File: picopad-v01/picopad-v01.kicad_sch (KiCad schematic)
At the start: 19 parts

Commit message: Complete the schematic
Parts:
- added D? (x17): SOD123, symbol Device:D_Small
- added MX?: NUMPAD_5, symbol MX-switches:MX-NoLED
- added MX?: NUMPAD_6, symbol MX-switches:MX-NoLED
- added MX?: NUMPAD_DOT, symbol MX-switches:MX-NoLED
- added MX?: NUMPAD_ASTERISK, symbol MX-switches:MX-NoLED
- added MX?: NUMPAD_PLUS, symbol MX-switches:MX-NoLED
- added MX?: NUMLOCK, symbol MX-switches:MX-NoLED
- added MX?: NUMPAD_1, symbol MX-switches:MX-NoLED
- added MX?: NUMPAD_7, symbol MX-switches:MX-NoLED
- added MX?: NUMPAD_MINUS, symbol MX-switches:MX-NoLED
- added MX?: NUMPAD_3, symbol MX-switches:MX-NoLED
- added MX?: NUMPAD_SLASH, symbol MX-switches:MX-NoLED
- added MX?: NUMPAD_4, symbol MX-switches:MX-NoLED
- added MX?: NUMPAD_ENTER, symbol MX-switches:MX-NoLED
- added MX?: NUMPAD_0, symbol MX-switches:MX-NoLED
- added MX?: NUMPAD_2, symbol MX-switches:MX-NoLED
- added MX?: NUMPAD_8, symbol MX-switches:MX-NoLED
- added MX?: NUMPAD_9, symbol MX-switches:MX-NoLED
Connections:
- net RGBLED: now reaches U?.11 (PB3)
- new net: D?.2 (A), MX?.2 (ROW) (x17)
- new net COL0: MX?.1 (COL), MX?.1 (COL), MX?.1 (COL), MX?.1 (COL), MX?.1 (COL), MX?.1 (COL), MX?.1 (COL), MX?.1 (COL), MX?.1 (COL), MX?.1 (COL), MX?.1 (COL), MX?.1 (COL), MX?.1 (COL), MX?.1 (COL), MX?.1 (COL), MX?.1 (COL), MX?.1 (COL)
- new net ROW0: D?.1 (K), D?.1 (K), D?.1 (K), D?.1 (K)
- new net ROW1: D?.1 (K), D?.1 (K), D?.1 (K)
- new net ROW2: D?.1 (K), D?.1 (K), D?.1 (K), D?.1 (K)
- new net ROW3: D?.1 (K), D?.1 (K), D?.1 (K)
- new net ROW4: D?.1 (K), D?.1 (K), D?.1 (K)

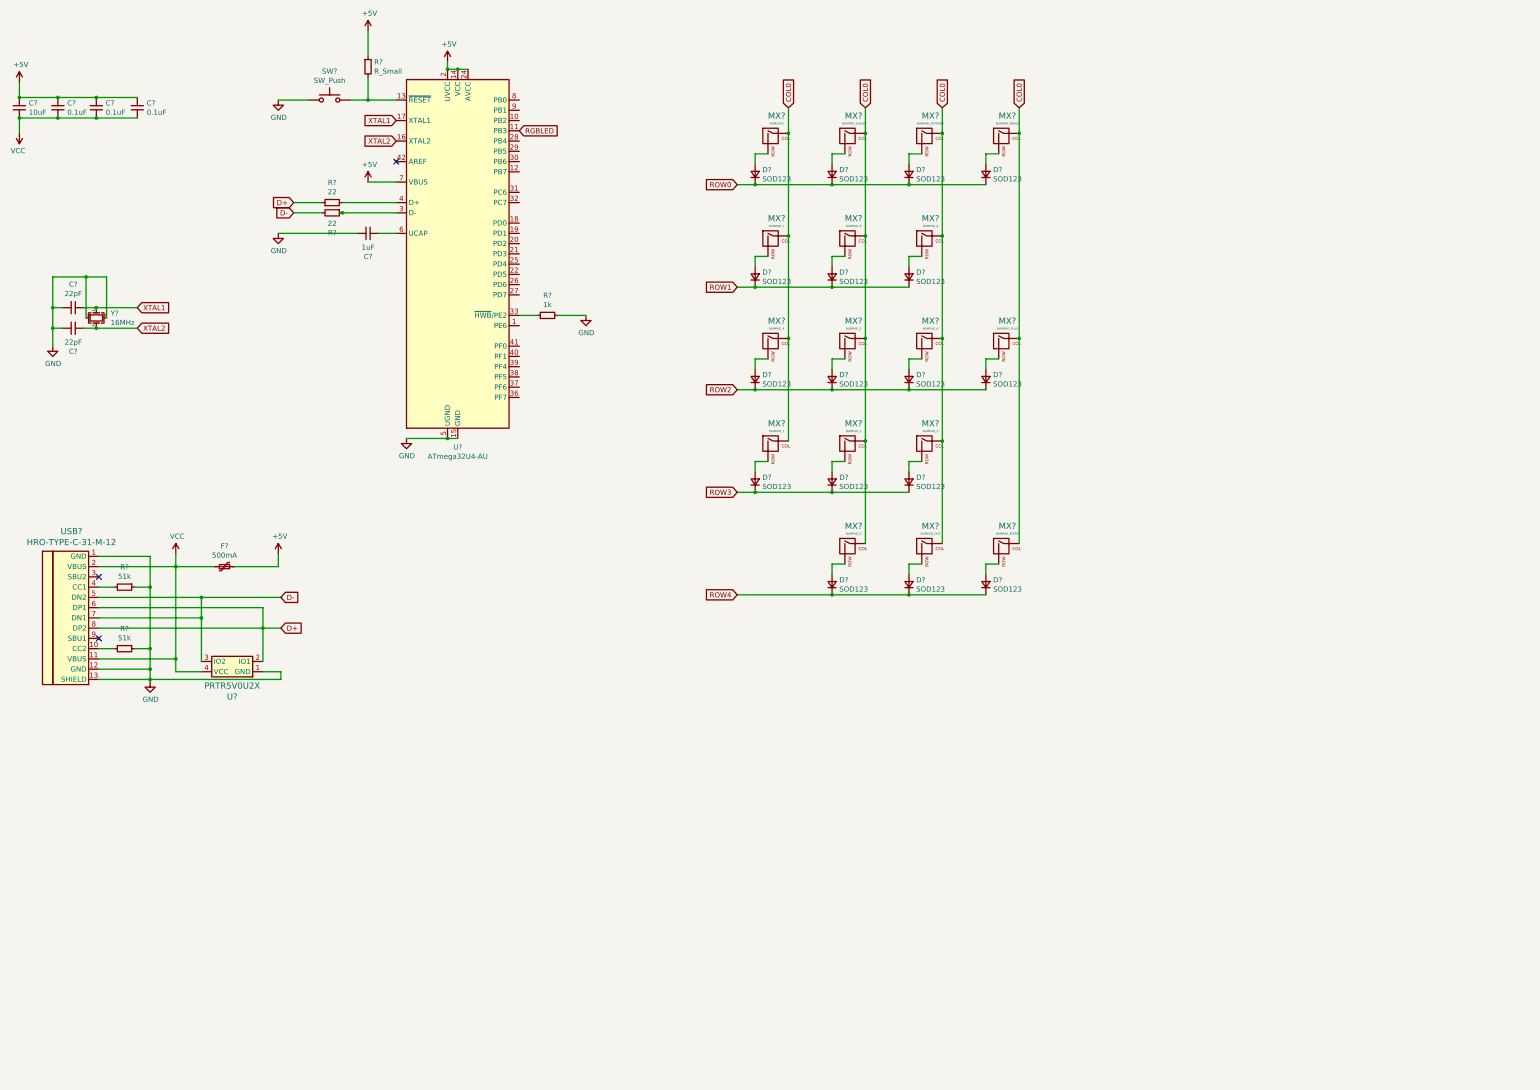
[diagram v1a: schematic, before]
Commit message: Add RGB backlight support
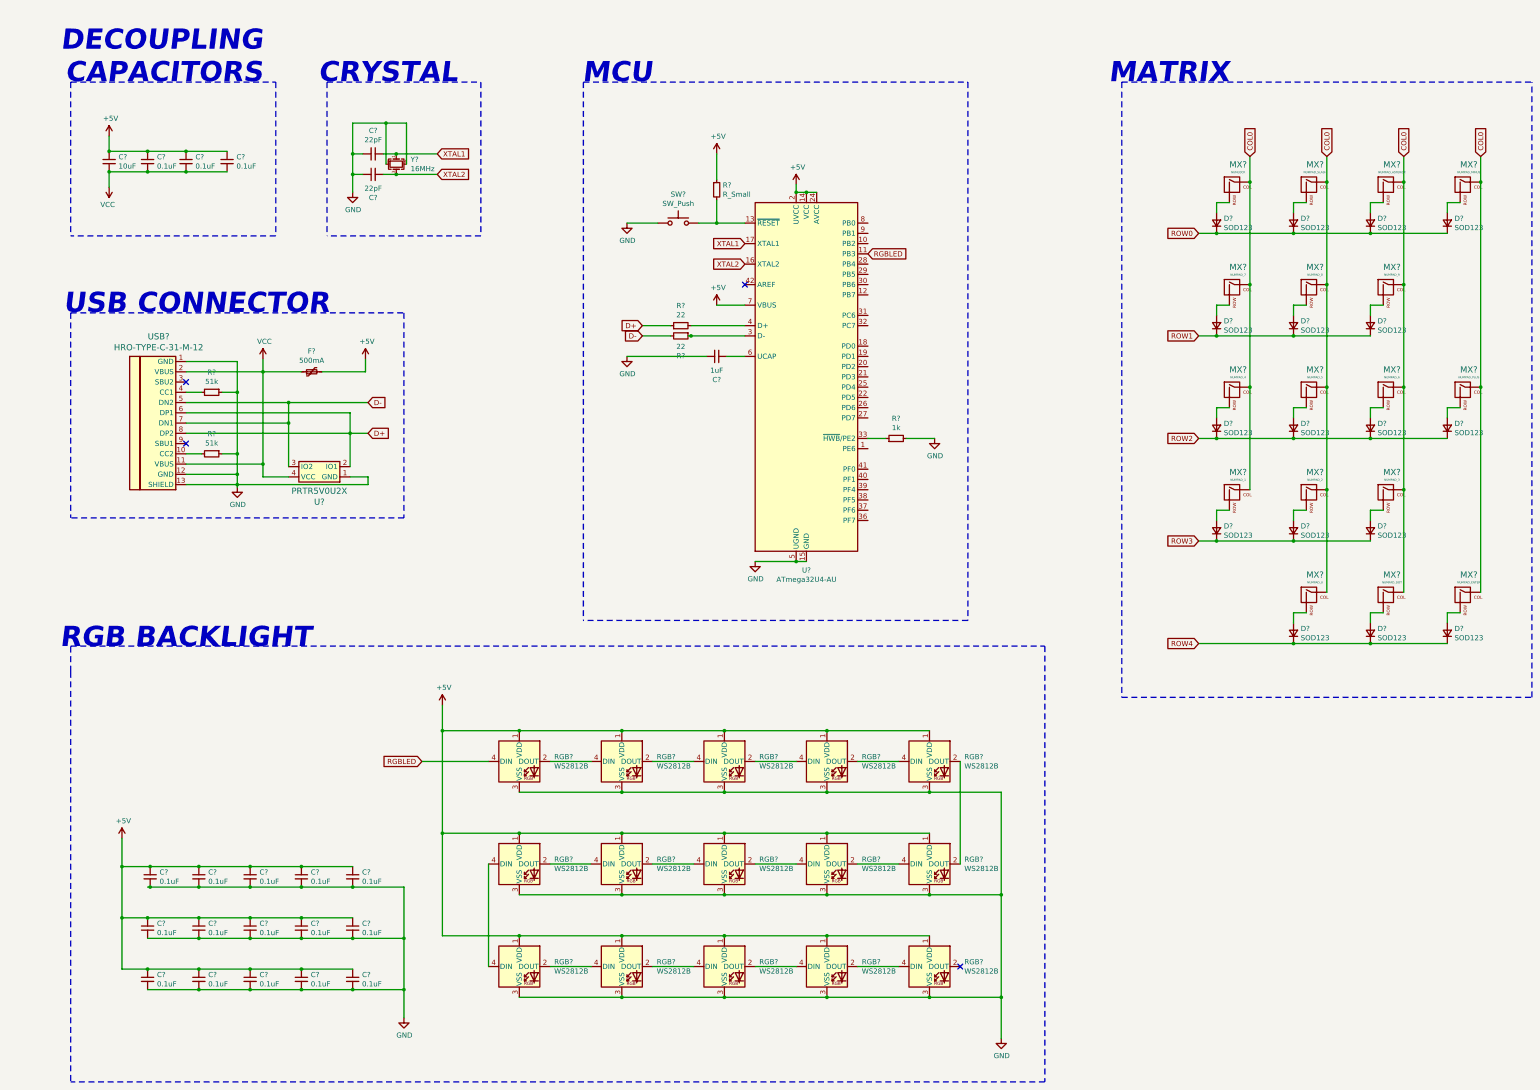
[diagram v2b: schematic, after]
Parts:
- added C? (x15): 0.1uF, symbol Device:C_Small
- added RGB? (x15): WS2812B, LED_SMD:LED_WS2812B_PLCC4_5.0x5.0mm_P3.2mm, symbol LED:WS2812B
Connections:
- net +5V: now also C?.1, C?.1, C?.1, C?.1, C?.1, C?.1, C?.1, C?.1, C?.1, C?.1, C?.1, C?.1, C?.1, C?.1, C?.1, RGB?.1 (VDD), RGB?.1 (VDD), RGB?.1 (VDD), RGB?.1 (VDD), RGB?.1 (VDD), RGB?.1 (VDD), RGB?.1 (VDD), RGB?.1 (VDD), RGB?.1 (VDD), RGB?.1 (VDD), RGB?.1 (VDD), RGB?.1 (VDD), RGB?.1 (VDD), RGB?.1 (VDD), RGB?.1 (VDD)
- net GND: now also C?.2, C?.2, C?.2, C?.2, C?.2, C?.2, C?.2, C?.2, C?.2, C?.2, C?.2, C?.2, C?.2, C?.2, C?.2, RGB?.3 (VSS), RGB?.3 (VSS), RGB?.3 (VSS), RGB?.3 (VSS), RGB?.3 (VSS), RGB?.3 (VSS), RGB?.3 (VSS), RGB?.3 (VSS), RGB?.3 (VSS), RGB?.3 (VSS), RGB?.3 (VSS), RGB?.3 (VSS), RGB?.3 (VSS), RGB?.3 (VSS), RGB?.3 (VSS)
- net RGBLED: now also RGB?.4 (DIN)
- new net: RGB?.2 (DOUT), RGB?.4 (DIN) (x12)
- new net: RGB?.4 (DIN), RGB?.4 (DIN)
- new net: RGB?.2 (DOUT), RGB?.2 (DOUT)
- no-connect marks 3 -> 4
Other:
- note added: "CRYSTAL"
- note added: "DECOUPLING CAPACITORS"
- note added: "MATRIX"
- note added: "MCU"
- note added: "RGB BACKLIGHT"
- note added: "USB CONNECTOR"
- title: (none) -> Picopad
- moved on the sheet: C?, D?, F?, MX?, R?, SW?, U?, USB?, Y?

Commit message: Complete the footprint assignment
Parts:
- C1, C2, C3, C4, C5, C6, C7: renamed from C?; footprint (none) -> Capacitor_SMD:C_0805_2012Metric
- C10, C11, C12, C13, C14, C15, C16, C17, C18, C19, C20, C21, C22, C8, C9: renamed from C?; footprint (none) -> Capacitor_SMD:C_0603_1608Metric
- D1, D10, D11, D12, D13, D14, D15, D16, D17, D2, D3, D4, D5, D6, D7, D8, D9: renamed from D?; footprint (none) -> Diode_SMD:D_SOD-123
- F1: renamed from F?; footprint (none) -> Fuse:Fuse_1206_3216Metric
- MX1, MX10, MX12, MX13, MX14, MX16, MX2, MX3, MX4, MX5, MX6, MX7, MX8, MX9: renamed from MX?; footprint (none) -> picopad:MXOnly-1U-Hotswap
- MX11, MX17: renamed from MX?; footprint (none) -> picopad:MXOnly-2U-Hotswap-Vertical
- MX15: renamed from MX?; footprint (none) -> picopad:MXOnly-2U-Hotswap
- R1: renamed from R?; value R_Small -> 10k; footprint (none) -> Resistor_SMD:R_0805_2012Metric
- R2, R3, R5, R6: renamed from R?; footprint (none) -> Resistor_SMD:R_0805_2012Metric
- R4: renamed from R?; value 1k -> 10k; footprint (none) -> Resistor_SMD:R_0805_2012Metric
- SW1: renamed from SW?; footprint (none) -> Random-keyboard-parts:SKQG-1155865
- U2: renamed from U?; footprint (none) -> Random-keyboard-parts:SOT143B
- USB1: renamed from USB?; footprint (none) -> Type-C:HRO-TYPE-C-31-M-12
- Y1: renamed from Y?; footprint (none) -> Crystal:Crystal_SMD_3225-4Pin_3.2x2.5mm
- gave numbers to parts that had none: 16

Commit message: Place the footprints on the PCB
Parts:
- added C23, C24: 0.1uF, Capacitor_SMD:C_0603_1608Metric, symbol Device:C_Small
- added RGB16, RGB17: WS2812B, picopad:WS2812B-3528, symbol LED:WS2812B
- RGB1, RGB10, RGB11, RGB12, RGB13, RGB14, RGB15, RGB2, RGB3, RGB4, RGB5, RGB6, RGB7, RGB8, RGB9: footprint LED_SMD:LED_WS2812B_PLCC4_5.0x5.0mm_P3.2mm -> picopad:WS2812B-3528
- renumbered D4 to D1, D9 to D10, D8 to D11, D17 to D15, D15 to D17, D3 to D2, D2 to D3, D1 to D4, D11 to D8, D10 to D9, MX4 to MX1, MX9 to MX10, MX8 to MX11, MX17 to MX15, MX15 to MX17, MX3 to MX2, MX2 to MX3, MX1 to MX4, MX11 to MX8, MX10 to MX9
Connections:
- net +5V: now also C23.1, C24.1, RGB16.1 (VDD), RGB17.1 (VDD)
- net GND: now also C2.2, C3.2, C4.2, C5.2, C23.2, C24.2, RGB16.3 (VSS), RGB17.3 (VSS)
- net VCC: no longer C2.2, C3.2, C4.2, C5.2
- net at RGB15.2 (DOUT): now also RGB16.2 (DOUT)
- new net: RGB16.4 (DIN), RGB17.2 (DOUT)
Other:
- moved on the sheet: C10, C11, C12, C13, C14, C15, C16, C17, C18, C19, C20, C21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
